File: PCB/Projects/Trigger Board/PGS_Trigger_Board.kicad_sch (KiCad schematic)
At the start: 3 parts, among them J1 Molex 505110-0492, SW1 EVQ-P0E07K, SW2 EVQ-P0E07K

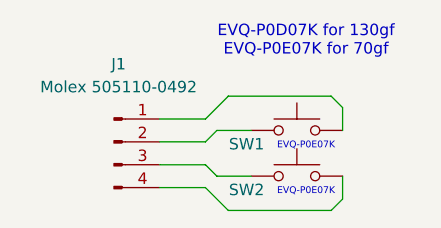
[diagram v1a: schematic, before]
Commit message: Main Board/Trigger Board Update
- Main board updated with Kailh tactile switches
- Trigger board updated with Kailh tactile switches
- USBW board updated to remove unneeded diode, move position of USB-C port
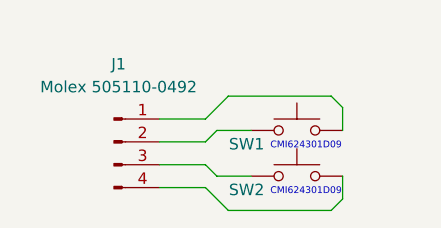
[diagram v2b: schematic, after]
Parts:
- SW1, SW2: value EVQ-P0E07K -> CMI624301D09; LCSC C395225 -> (none); MPN EVQ-P0E07K -> CMI624301D09; Manufacturer PANASONIC -> Kailh
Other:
- note added: "CMI624301D09"
- note removed: "EVQ-P0D07K for 130gf EVQ-P0E07K for 70gf"
- note removed: "EVQ-P0E07K"
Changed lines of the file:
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@@
 		(company "Hand Held Legend, LLC")
 	)
-	(text "EVQ-P0E07K"
+	(text "CMI624301D09"
 		(exclude_from_sim no)
 		(at 73.406 32.258 0)
@@
 		)
 	)
-	(text "EVQ-P0D07K for 130gf\nEVQ-P0E07K for 70gf"
-		(exclude_from_sim no)
-		(at 73.406 15.494 0)
-		(effects
-			(font
-				(size 1.27 1.27)
-			)
-		)
-	)
-	(text "EVQ-P0E07K"
+	(text "CMI624301D09"
 		(exclude_from_sim no)
 		(at 73.406 27.178 0)
@@
 			)
 		)
-		(property "Value" "EVQ-P0E07K"
+		(property "Value" "CMI624301D09"
 			(at 72.39 25.4 0)
 			(effects
@@
 			)
 		)
-		(property "MPN" "EVQ-P0E07K"
+		(property "MPN" "CMI624301D09"
 			(at 72.39 30.48 0)
 			(effects
@@
 			)
 		)
-		(property "LCSC" "C395225"
+		(property "LCSC" ""
 			(at 72.39 30.48 0)
 			(effects
@@
 			)
 		)
-		(property "Manufacturer" "PANASONIC"
+		(property "Manufacturer" "Kailh"
 			(at 72.39 30.48 0)
 			(effects
@@
 			)
 		)
-		(property "Value" "EVQ-P0E07K"
+		(property "Value" "CMI624301D09"
 			(at 72.39 20.32 0)
 			(effects
@@
 			)
 		)
-		(property "Datasheet" "~"
+		(property "Datasheet" "https://uelectronics.com/wp-content/uploads/2024/12/Datasheet-Microinterruptor-Silencioso-para-Mouse-CMI624301D09.pdf?srsltid=AfmBOop6n-LI93civhddjTPUOZCj3iSyUFg8_0Vf9y402ymvABNEZW8f"
 			(at 72.39 20.32 0)
 			(effects
@@
 			)
 		)
-		(property "MPN" "EVQ-P0E07K"
+		(property "MPN" "CMI624301D09"
 			(at 72.39 25.4 0)
 			(effects
@@
 			)
 		)
-		(property "LCSC" "C395225"
+		(property "LCSC" ""
 			(at 72.39 25.4 0)
 			(effects
@@
 			)
 		)
-		(property "Manufacturer" "PANASONIC"
-			(at 72.39 25.4 0)
-			(effects
+		(property "Manufacturer" "Kailh"
+			(at 72.39 25.4 0)
+			(effects
